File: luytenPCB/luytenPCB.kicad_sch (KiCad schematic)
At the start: 36 parts, among them IC1 DRV8212DRLR, IC2 DRV8212DRLR, J1 Battery, J10 START_M, J2 BDC1, J3 BDC2, J4 LINE_RF, J5 LINE_LF, J6 DIST_L, J7 DIST_LM, J8 DIST_R, J9 DIST_RM, SW1 SW_SPST, SW2 ProgSelect

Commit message: pcb production prototype done
finished schematic and layout
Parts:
- added H1, H2, H3, H4: MountingHole, MountingHole:MountingHole_2.2mm_M2_ISO7380, symbol Mechanical:MountingHole
- F1: value Fuse -> 15A; footprint (none) -> Fuse:Fuse_1206_3216Metric_Pad1.42x1.75mm_HandSolder
- J1: footprint Connector_AMASS:AMASS_XT30PW-M_1x02_P2.50mm_Horizontal -> Connector_AMASS:AMASS_XT30U-M_1x02_P5.0mm_Vertical
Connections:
- net +12V: now also F1.2; no longer F1.1
- net MDC1_1: now also A1.D2; no longer A1.D3
- net MDC1_2: now also A1.D3; no longer A1.D2
- net MDC2_1: now also A1.D11 (D11_MOSI); no longer A1.D12 (D12_MISO)
- net MDC2_2: now also A1.D12 (D12_MISO); no longer A1.D11 (D11_MOSI)
- net at SW1.1 (A): now also F1.1; no longer F1.2
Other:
- moved on the sheet: F1, SW2

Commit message: updates
--fixes to routing, updated screw terminal
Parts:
- added D7: GREEN, Capacitor_SMD:C_0603_1608Metric_Pad1.08x0.95mm_HandSolder, symbol Device:LED
- added J11: DIST_C, Connector_PinHeader_2.54mm:PinHeader_1x03_P2.54mm_Vertical, symbol Connector_Generic:Conn_02x02_Odd_Even
- added R7: 100, Diode_SMD:D_0805_2012Metric_Pad1.15x1.40mm_HandSolder, symbol Device:R_US
- J2, J3: footprint Connector_Phoenix_MSTB:PhoenixContact_MSTBA_2,5_2-G_1x02_P5.00mm_Horizontal -> Connector_PinHeader_2.54mm:PinHeader_1x02_P2.54mm_Vertical
- J4, J5, J6, J7, J8, J9: footprint Connector_Phoenix_MSTB:PhoenixContact_MSTBA_2,5_3-G_1x03_P5.00mm_Horizontal -> Connector_PinHeader_2.54mm:PinHeader_1x03_P2.54mm_Vertical
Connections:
- net +3.3V: now also J11.1 (Pin_1)
- net GND: now also J1.1 (Pin_1), D7.1 (K), J11.3 (Pin_3); no longer J1.2 (Pin_2)
- net MDC1_1: now also A1.A6; no longer A1.D2
- net MDC1_2: now also A1.A7; no longer A1.D3
- net MDC2_1: now also A1.A4 (A4/SDA); no longer A1.D11 (D11_MOSI)
- net MDC2_2: now also A1.A5 (A5/SCL); no longer A1.D12 (D12_MISO)
- net at SW1.2 (B): now also J1.2 (Pin_2); no longer J1.1 (Pin_1)
- net DIST_C_INT: now reaches A1.D9
- net DIST_C_INT: now also J11.2 (Pin_2), R7.1
- new net: D7.2 (A), R7.2
- no-connect marks 12 -> 11
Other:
- moved on the sheet: D3, D4, D5, D6, J1, R3, R4, R5, R6

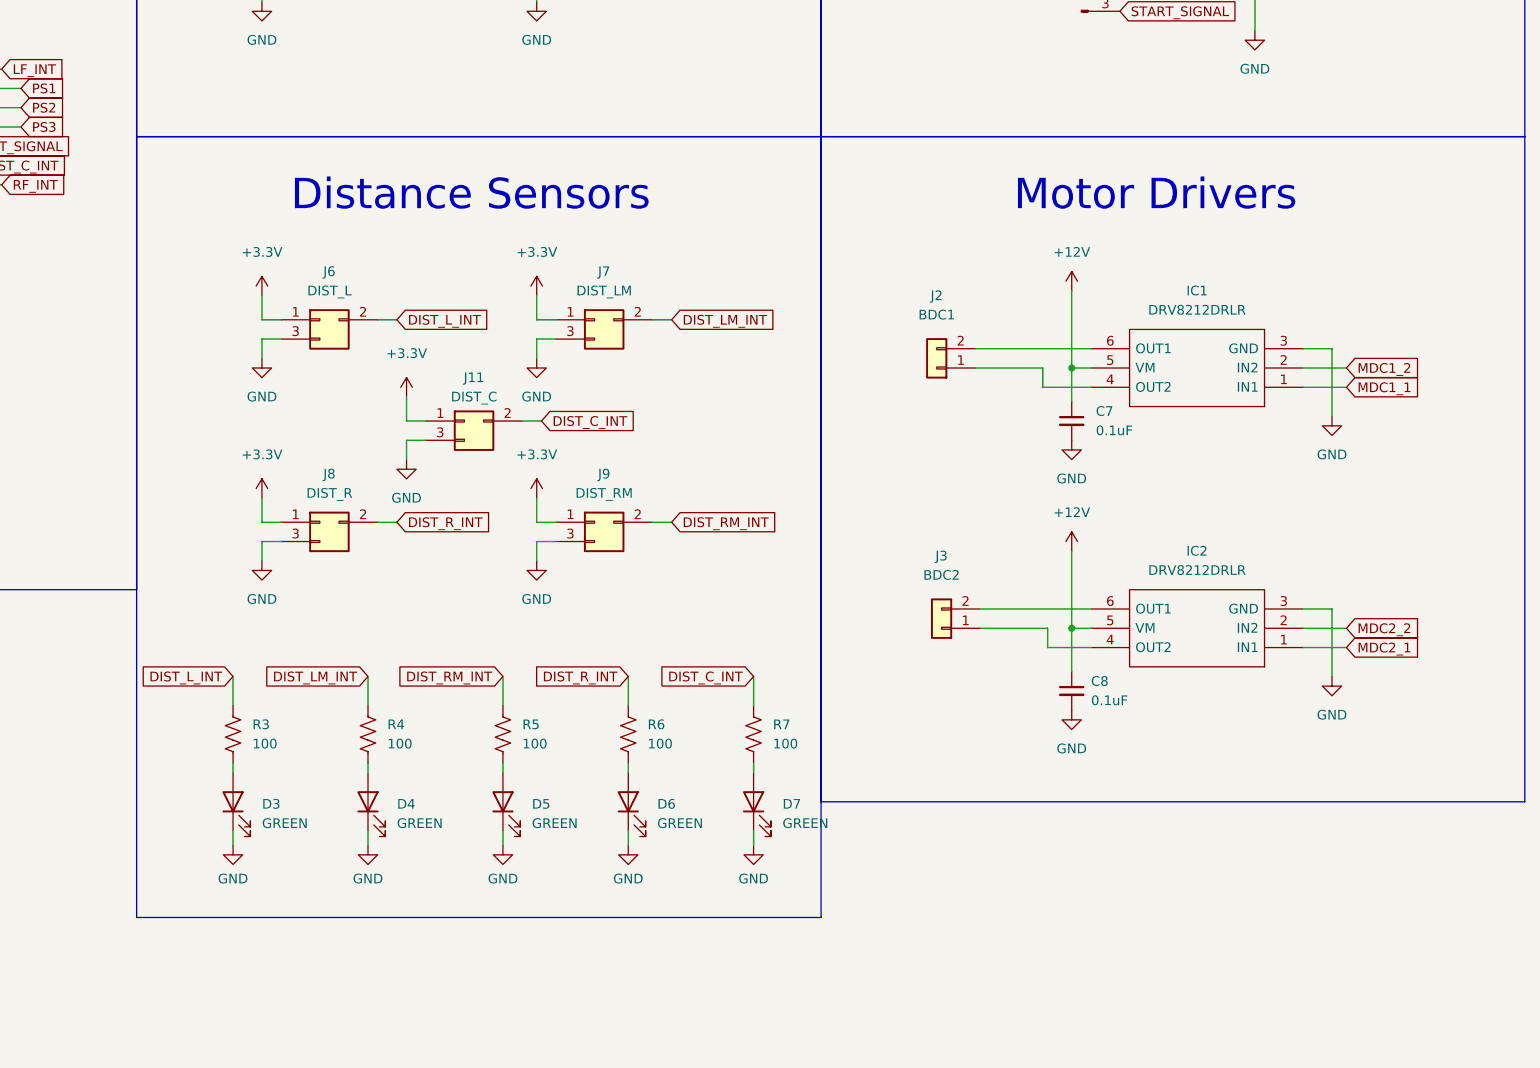
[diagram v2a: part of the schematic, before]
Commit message: luytenv2
forgot to update spst footprint :(
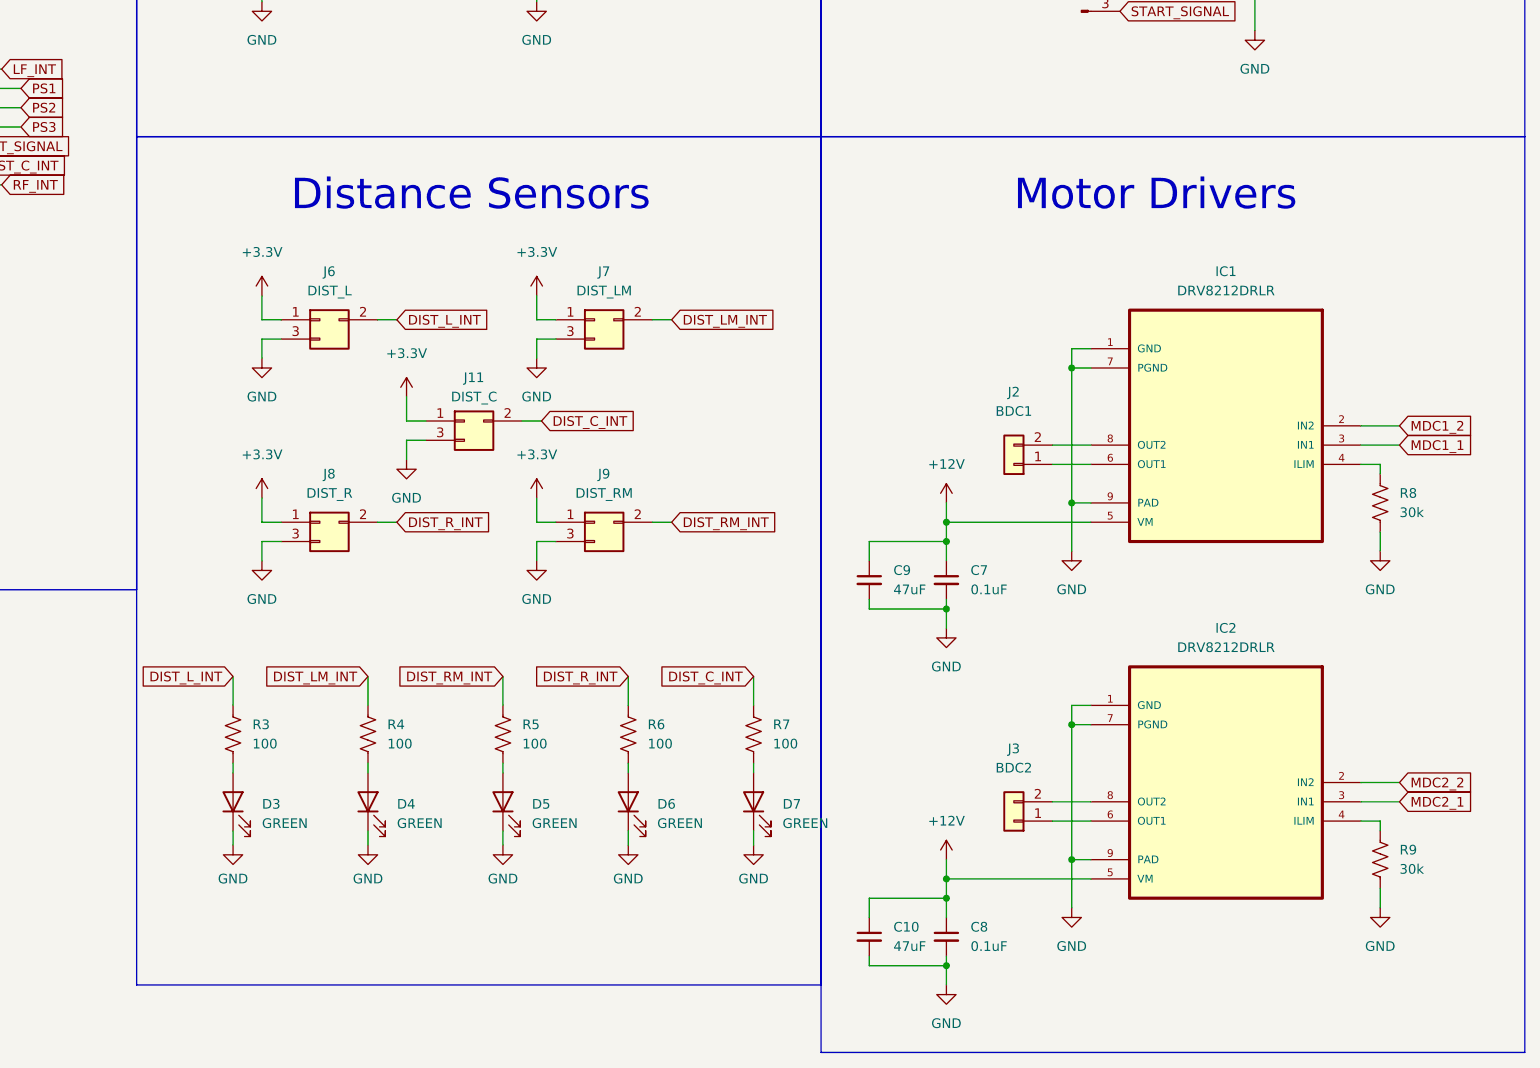
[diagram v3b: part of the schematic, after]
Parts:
- added C10, C9: 47uF, Capacitor_SMD:C_0805_2012Metric_Pad1.18x1.45mm_HandSolder, symbol Device:C_Small
- added R8, R9: 30k, Diode_SMD:D_0805_2012Metric_Pad1.15x1.40mm_HandSolder, symbol Device:R_US
- IC1, IC2: footprint Package_TO_SOT_SMD:SOT-563 -> DRV8871DDAR:VREG_LM5017MR_NOPB; symbol DRV8212DRLR:DRV8212DRLR -> DRV8871DDAR:DRV8871DDAR; Availability (none) -> In Stock; Check_prices (none) -> https://www.snapeda.com/parts/DRV8871DDAR/Texas+Instruments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; MF (none) -> Texas Instruments; MP (none) -> DRV8871DDAR; Package (none) -> HSOIC-8 Texas Instruments; Price (none) -> None; Purchase-URL (none) -> https://www.snapeda.com/api/url_track_click_mouser/?unipart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; SnapEDA_Link (none) -> https://www.snapeda.com/parts/DRV8871DDAR/Texas+Instruments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
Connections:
- net +12V: now also C10.1, C9.1
- net GND: now also IC1.1 (GND), IC1.7 (PGND), IC1.9 (PAD), IC2.1 (GND), IC2.7 (PGND), IC2.9 (PAD), C10.2, C9.2, R8.2, R9.2; no longer IC1.3 (GND), IC2.3 (GND)
- net MDC1_1: now also IC1.3 (IN1); no longer IC1.1 (IN1)
- net MDC2_1: now also IC2.3 (IN1); no longer IC2.1 (IN1)
- net at J3.1 (Pin_1): now also IC2.6 (OUT1); no longer IC2.4 (OUT2)
- net at J3.2 (Pin_2): now also IC2.8 (OUT2); no longer IC2.6 (OUT1)
- net at IC1.4 (ILIM): now also R8.1; no longer J2.1 (Pin_1)
- net at IC1.6 (OUT1): now also J2.1 (Pin_1); no longer J2.2 (Pin_2)
- new net: IC2.4 (ILIM), R9.1
- new net: IC1.8 (OUT2), J2.2 (Pin_2)
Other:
- moved on the sheet: C7, J2, J3
